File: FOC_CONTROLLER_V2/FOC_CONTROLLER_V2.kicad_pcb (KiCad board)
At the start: 4 copper layers, 80 x 60 mm, 124 parts, among them IC1 STSPIN32G4, J1 DC IN, J2 Conn_01x01, J3 Conn_01x01, J4 Conn_01x01, J5 ENCODER, J6 JTAG, Q1 CSD18502Q5B, Q2 CSD18502Q5B, Q3 CSD18502Q5B, Q4 CSD18502Q5B, Q5 CSD18502Q5B, Q6 CSD18502Q5B, SW3 SW_DIP_x02, U1 THVD1520

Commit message: Routage Phases PCB
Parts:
- removed C23: N.M., Capacitor_SMD:C_0603_1608Metric
- removed the R14 at (70.7, 79.0)
- removed the R15 at (70.7, 81.5)
- removed the R16 at (70.7, 84.0)
- removed the R17 at (70.7, 86.5)
- removed the R18 at (70.7, 89.0)
- removed Rshunt1, Rshunt2, Rshunt3: 7m, Resistor_SMD:R_2512_6332Metric_Pad1.40x3.35mm_HandSolder
- removed TP1, TP2, TP21, TP3, TP4: 3V3, TestPoint:TestPoint_Pad_D1.0mm
- removed TP10, TP11, TP12, TP13, TP14, TP15, TP16, TP17, TP18, TP20, TP5, TP6, TP7, TP8, TP9: 5V, TestPoint:TestPoint_Pad_D1.0mm
- removed TP19: 24V, TestPoint:TestPoint_Pad_D1.0mm
- added C25: N.M., Capacitor_SMD:C_1210_3225Metric_Pad1.33x2.70mm_HandSolder, B.Cu at (156.2, 85.1)
- added C26: N.M., Capacitor_SMD:C_1210_3225Metric_Pad1.33x2.70mm_HandSolder, B.Cu at (140.6, 85.1)
- added C27: N.M., Capacitor_SMD:C_1210_3225Metric_Pad1.33x2.70mm_HandSolder, B.Cu at (135.6, 88.3)
- added C28: 100n, Capacitor_SMD:C_0603_1608Metric, F.Cu at (141.8, 111.1)
- added C29: 100n, Capacitor_SMD:C_0603_1608Metric, F.Cu at (220.7, 71.0)
- added C30: 220n, Capacitor_SMD:C_0603_1608Metric, F.Cu at (220.7, 73.5)
- added C31: N.M., Capacitor_SMD:C_1210_3225Metric_Pad1.33x2.70mm_HandSolder, B.Cu at (146.2, 85.1)
- added C32: N.M., Capacitor_SMD:C_1210_3225Metric_Pad1.33x2.70mm_HandSolder, B.Cu at (130.5, 85.1)
- added C33: N.M., Capacitor_SMD:C_1210_3225Metric_Pad1.33x2.70mm_HandSolder, B.Cu at (151.2, 85.1)
- added C34: N.M., Capacitor_SMD:C_1210_3225Metric_Pad1.33x2.70mm_HandSolder, B.Cu at (146.2, 88.3)
- added D4: STPS0560Z, Diode_SMD:D_SOD-123, F.Cu at (158.3, 108.8)
- added J10: R-78B5.0-2.0, Package_TO_SOT_SMD:SOT-223, F.Cu at (130.1, 128.6)
- added J7: Conn_SW_2, Connector_JST:JST_GH_SM02B-GHS-TB_1x02-1MP_P1.25mm_Horizontal, F.Cu at (196.1, 94.5)
- added J8: Conn_SW_2, Connector_JST:JST_GH_SM02B-GHS-TB_1x02-1MP_P1.25mm_Horizontal, F.Cu at (188.3, 108.2)
- added J9: USB_C_Receptacle_USB2.0_14P, Connector_USB:USB_C_Receptacle_G-Switch_GT-USB-7010ASV, F.Cu at (103.6, 116.6)
- added JP1: SolderJumper_3_Open, Jumper:SolderJumper-3_P1.3mm_Open_RoundedPad1.0x1.5mm_NumberLabels, F.Cu at (126.3, 121.9)
- added L1: 15u, Footprint:L_Wurth_WE-MXGI-5030, F.Cu at (159.3, 113.1)
- added R14: 30K, Resistor_SMD:R_0603_1608Metric, F.Cu at (133.5, 84.6)
- added R14: 30K, Resistor_SMD:R_0603_1608Metric, F.Cu at (267.0, 84.4)
- added R15: 30K, Resistor_SMD:R_0603_1608Metric, F.Cu at (265.4, 87.4)
- added R15: 30K, Resistor_SMD:R_0603_1608Metric, F.Cu at (132.0, 87.6)
- added R16: 1.5k, Resistor_SMD:R_0603_1608Metric, F.Cu at (130.4, 84.6)
- added R16: 1.5k, Resistor_SMD:R_0603_1608Metric, F.Cu at (263.8, 84.4)
- added R17: 15k, Resistor_SMD:R_0603_1608Metric, F.Cu at (263.8, 87.4)
- added R17: 15k, Resistor_SMD:R_0603_1608Metric, F.Cu at (130.4, 87.6)
- added R18: 1.5k, Resistor_SMD:R_0603_1608Metric, F.Cu at (132.0, 84.6)
- added R18: 1.5k, Resistor_SMD:R_0603_1608Metric, F.Cu at (265.4, 84.4)
- added R49: 100k, Capacitor_SMD:C_0603_1608Metric, F.Cu at (145.0, 111.1)
- added R50: 200, Capacitor_SMD:C_0603_1608Metric, F.Cu at (145.0, 113.6)
- added R51: 100k, Capacitor_SMD:C_0603_1608Metric, F.Cu at (228.8, 73.5)
- added R52: 200, Capacitor_SMD:C_0603_1608Metric, F.Cu at (228.8, 76.0)
- added R53: 10, Resistor_SMD:R_0603_1608Metric, F.Cu at (115.5, 116.6)
- C1, C3, C5: footprint Capacitor_SMD:C_0603_1608Metric -> Capacitor_SMD:C_0805_2012Metric
- C13: value N.M. -> 10u
- C17: footprint Capacitor_SMD:C_0201_0603Metric -> Capacitor_SMD:C_0603_1608Metric
- C19: value 4u7 -> 10u; footprint Capacitor_SMD:C_1210_3225Metric -> Capacitor_SMD:C_0805_2012Metric_Pad1.18x1.45mm_HandSolder
- C20: value 4u7 -> 22u; footprint Capacitor_SMD:C_1210_3225Metric -> Capacitor_SMD:C_0805_2012Metric_Pad1.18x1.45mm_HandSolder
- C21: value 1u -> N.M.; footprint Capacitor_SMD:C_0603_1608Metric -> Capacitor_SMD:C_1210_3225Metric_Pad1.33x2.70mm_HandSolder; moved to B.Cu
- C22: value 47u -> N.M.; footprint Capacitor_SMD:C_0603_1608Metric -> Capacitor_SMD:C_1210_3225Metric_Pad1.33x2.70mm_HandSolder; moved to B.Cu
- C4, C6, C7: value 220n 100V -> 220n; footprint Capacitor_SMD:C_0805_2012Metric -> Capacitor_SMD:C_1210_3225Metric_Pad1.33x2.70mm_HandSolder; moved to B.Cu
- J2, J3, J4: footprint Footprint:REDCUBE SMT -> Footprint:REDCUBETHT_74651173R
- J5: footprint Connector_JST:JST_SH_SM04B-SRSS-TB_1x04-1MP_P1.00mm_Horizontal -> Connector_JST:JST_GH_SM04B-GHS-TB_1x04-1MP_P1.25mm_Horizontal
- Q1, Q4, Q6: value CSD18502Q5B -> CSD18543Q3A; moved to B.Cu
- Q2, Q3, Q5: value CSD18502Q5B -> CSD19534Q5A; moved to B.Cu
- R31: value 5k6 -> R_Shunt; footprint Resistor_SMD:R_0402_1005Metric -> shunt:R_2512_6332Metric_Pad1.40x3.35mm_HandSolder
- R32: value 402k -> R_Shunt; footprint Resistor_SMD:R_0402_1005Metric -> shunt:R_2512_6332Metric_Pad1.40x3.35mm_HandSolder
- R33: value 80k6 -> R_Shunt; footprint Resistor_SMD:R_0402_1005Metric -> shunt:R_2512_6332Metric_Pad1.40x3.35mm_HandSolder
- U1: value THVD1520 -> THVD1400
- moved R38 205.3 mm to (236.3, 84.0)
- moved R39 205.3 mm to (236.3, 86.0)
- moved R40 203.1 mm to (236.3, 88.0)
- moved C18 202.7 mm to (216.7, 83.6)
- moved NTC1 202.7 mm to (220.7, 76.0)
- moved R2 202.7 mm to (220.7, 78.6)
- moved R8 202.7 mm to (220.7, 81.1)
- moved R9 202.7 mm to (220.7, 83.6)
- moved C10 202.7 mm to (216.7, 68.5)
- moved C11 202.7 mm to (216.7, 71.0)
- moved C12 202.7 mm to (216.7, 73.5)
- moved C14 202.7 mm to (216.7, 76.0)
- moved C15 202.7 mm to (216.7, 78.6)
- moved C9 202.7 mm to (216.7, 66.0)
- moved R10 202.7 mm to (224.8, 66.0)
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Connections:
- net A renamed /A
- net B renamed /B
- C13 pad 1: /OPN2 -> Net-(IC1-REGIN)
- C13 pad 2: /OPO2 -> GND
- C16 pad 1: /OPN3 -> Net-(IC1-REGIN)
- C16 pad 2: /OPO3 -> GND
- C19 pad 1: +24V -> +5V
- C2 pad 1: +24V -> +48V
- C20 pad 1: +24V -> +3,3V_EXT
- C21 pad 1: Net-(PS1-VCC) -> GND
- C21 pad 2: Net-(PS1-AGND) -> +48V
- C22 pad 1: +5V -> GND
- C22 pad 2: Net-(PS1-AGND) -> +48V
- C4 pad 2: +24V -> +48V
- C6 pad 2: +24V -> +48V
- C7 pad 2: +24V -> +48V
- C8 pad 1: +24V -> +48V
- IC1 pad 14: /OPP1 -> /OPP3
- IC1 pad 15: /OPO1 -> /OPO3
- IC1 pad 16: /OPN1 -> /OPN3
- IC1 pad 23: /OPP3 -> /OPP1
- IC1 pad 24: /OPO3 -> /OPO1
- IC1 pad 25: /OPN3 -> /OPN1
- IC1 pad 59: unconnected-(IC1-PB8-Pad59) -> /L_SW_2
- IC1 pad 60: unconnected-(IC1-PB9-Pad60) -> /L_SW_1
- IC1 pad 61: +24V -> +48V
- IC1 pad 62: +24V -> /SW
- IC1 pad 63: +5V -> Net-(IC1-REGIN)
- IC1 pad 64: +5V -> Net-(IC1-REGIN)
- J1 pad 1: +24V -> +48V
- Q1 pad 1: /Ampli_1/VSHUNTXP -> Net-(Q1-S-Pad1)
- Q1 pad 2: /Ampli_1/VSHUNTXP -> Net-(Q1-S-Pad1)
- Q1 pad 3: /Ampli_1/VSHUNTXP -> Net-(Q1-S-Pad1)
- Q2 pad 5: +24V -> +48V
- Q3 pad 5: +24V -> +48V
- Q4 pad 1: /Ampli_2/VSHUNTXP -> Net-(Q4-S-Pad1)
- Q4 pad 2: /Ampli_2/VSHUNTXP -> Net-(Q4-S-Pad1)
- Q4 pad 3: /Ampli_2/VSHUNTXP -> Net-(Q4-S-Pad1)
- Q5 pad 5: +24V -> +48V
- Q6 pad 1: /Ampli_3/VSHUNTXP -> Net-(Q6-S-Pad1)
- Q6 pad 2: /Ampli_3/VSHUNTXP -> Net-(Q6-S-Pad1)
- Q6 pad 3: /Ampli_3/VSHUNTXP -> Net-(Q6-S-Pad1)
- R13 pad 1: GND -> /Ampli_2/VSHUNTXN
- R23 pad 1: GND -> /Ampli_3/VSHUNTXN
- R28 pad 1: +24V -> +48V
- R31 pad 1: Net-(PS1-FSW) -> GND
- R31 pad 2: Net-(PS1-AGND) -> /Ampli_1/VSHUNTXN
- R32 pad 1: +5V -> GND
- R32 pad 2: Net-(PS1-FB) -> /Ampli_2/VSHUNTXN
- R33 pad 1: Net-(PS1-FB) -> GND
- R33 pad 2: Net-(PS1-AGND) -> /Ampli_3/VSHUNTXN
- U1 pad 8: +5V -> Net-(JP1-C)
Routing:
- net /OUT3: track 0.00 -> 39.3 mm, vias 0 -> 1
- net GND: track 0.00 -> 36.4 mm, vias 0 -> 30
- net /OUT2: track 0.00 -> 29.2 mm, vias 0 -> 1
- net /OUT1: track 0.00 -> 20.1 mm, vias 0 -> 1
- net /A: track 0.00 -> 16.1 mm
- net /B: track 0.00 -> 15.6 mm, vias 0 -> 2
- net /GHS2: track 0.00 -> 14.5 mm, vias 0 -> 1
- net /Ampli_3/VSHUNTXP: track 0.00 -> 14.3 mm
- net /Ampli_3/VSHUNTXN: track 0.00 -> 11.9 mm
- net /Ampli_2/VSHUNTXP: track 0.00 -> 7.91 mm
- net /Ampli_2/VSHUNTXN: track 0.00 -> 7.71 mm
- net /Ampli_1/VSHUNTXP: track 0.00 -> 6.86 mm
- net Net-(JP1-C): track 0.00 -> 6.44 mm
- net +3,3V_EXT: track 0.00 -> 6.37 mm
- net /Ampli_1/VSHUNTXN: track 0.00 -> 4.52 mm
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- added copper zone on B.Cu, net +48V
- added copper zone on B.Cu, net /OUT1
- added copper zone on B.Cu, net /OUT2
- added copper zone on B.Cu, net /OUT3
- added copper zone on F.Cu, net GND
- added copper zone on In1.Cu, net GND
- added copper zone on In2.Cu, net GND
- added copper zone on B.Cu, net Net-(Q1-S-Pad1)
- added copper zone on F.Cu, net Net-(Q1-S-Pad1)
- added copper zone on B.Cu, net Net-(Q4-S-Pad1)
- added copper zone on F.Cu, net Net-(Q4-S-Pad1)
- added copper zone on B.Cu, net Net-(Q6-S-Pad1)
- added copper zone on F.Cu, net Net-(Q6-S-Pad1)
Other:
- board size 80 x 60 mm -> 80 x 80 mm

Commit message: Routage PCB 99%
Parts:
- removed C25, C34: N.M., Capacitor_SMD:C_1210_3225Metric_Pad1.33x2.70mm_HandSolder
- removed C7: 220n, Capacitor_SMD:C_1210_3225Metric_Pad1.33x2.70mm_HandSolder
- removed the R14 at (267.0, 84.4)
- removed the R15 at (265.4, 87.4)
- removed the R16 at (263.8, 84.4)
- removed the R17 at (263.8, 87.4)
- removed the R18 at (265.4, 84.4)
- C2: footprint Capacitor_SMD:CP_Elec_10x10.5 -> Capacitor_SMD:CP_Elec_18x22
- C21, C22, C26, C27, C31, C32, C33, C4, C6: moved to F.Cu
- J10: value R-78B5.0-2.0 -> AZ1117
- moved R48 136.1 mm to (108.8, 130.4), turned to 180 degrees
- moved D3 134.4 mm to (105.6, 130.4)
- moved D1 133.9 mm to (105.6, 126.2)
- moved R11 129.5 mm to (108.8, 126.2), turned to 180 degrees
- moved D5 128.0 mm to (107.8, 62.1), turned to 180 degrees
- moved R40 127.6 mm to (111.3, 62.1)
- moved R38 105.0 mm to (143.6, 133.5)
- moved C30 104.8 mm to (128.6, 123.5)
- moved C8 101.6 mm to (142.7, 114.0), turned to -90 degrees
- moved D8 101.5 mm to (140.1, 133.5), turned to 180 degrees
- moved R35 99.7 mm to (130.5, 116.0)
- moved R10 99.2 mm to (138.3, 114.6), turned to 90 degrees
- moved R39 98.9 mm to (149.5, 133.5), turned to 180 degrees
- moved R34 98.4 mm to (133.3, 117.5)
- moved D9 88.8 mm to (153.0, 133.5)
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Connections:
- D5 pad 2: +24V -> +48V
- IC1 pad 47: /DRIVE_EN -> /RECIEVE_EN
- IC1 pad 48: /RECIEVE_EN -> /DRIVE_EN
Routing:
- net /VCP_RX: track 0.00 -> 82.2 mm, vias 0 -> 2
- net /VCP_TX: track 0.00 -> 76.6 mm, vias 0 -> 2
- net Net-(IC1-PB3): track 0.00 -> 65.7 mm, vias 0 -> 2
- net Net-(IC1-PB5): track 0.00 -> 64.5 mm, vias 0 -> 2
- net Net-(IC1-PD2): track 0.00 -> 64.3 mm, vias 0 -> 2
- net /NTC: track 0.00 -> 63.7 mm, vias 0 -> 2
- net Net-(Q2-G): track 1.09 -> 64.5 mm, vias 0 -> 2
- net Net-(IC1-PB4): track 0.00 -> 59.9 mm, vias 0 -> 2
- net Net-(IC1-PC15): track 0.00 -> 55.5 mm, vias 0 -> 2
- net /NRST: track 0.00 -> 52.2 mm, vias 0 -> 2
- net Net-(Q5-G): track 0.00 -> 50.8 mm, vias 0 -> 2
- net Net-(Q3-G): track 0.00 -> 49.7 mm, vias 0 -> 2
- net Net-(IC1-PC14): track 0.00 -> 48.0 mm, vias 0 -> 2
- net /L_SW_1: track 0.00 -> 46.1 mm, vias 0 -> 2
- net /OUT2: track 29.2 -> 73.8 mm
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- added copper zone on B.Cu, net +3.3V
- added copper zone on F.Cu, net +3.3V
- added copper zone on F.Cu, net +48V
- added copper zone on B.Cu, net +5V
- added copper zone on F.Cu, net +5V
- added copper zone on F.Cu, net /SW
- added copper zone on F.Cu, net Net-(IC1-REGIN)
- added copper zone on F.Cu, net Net-(IC1-SCREF)

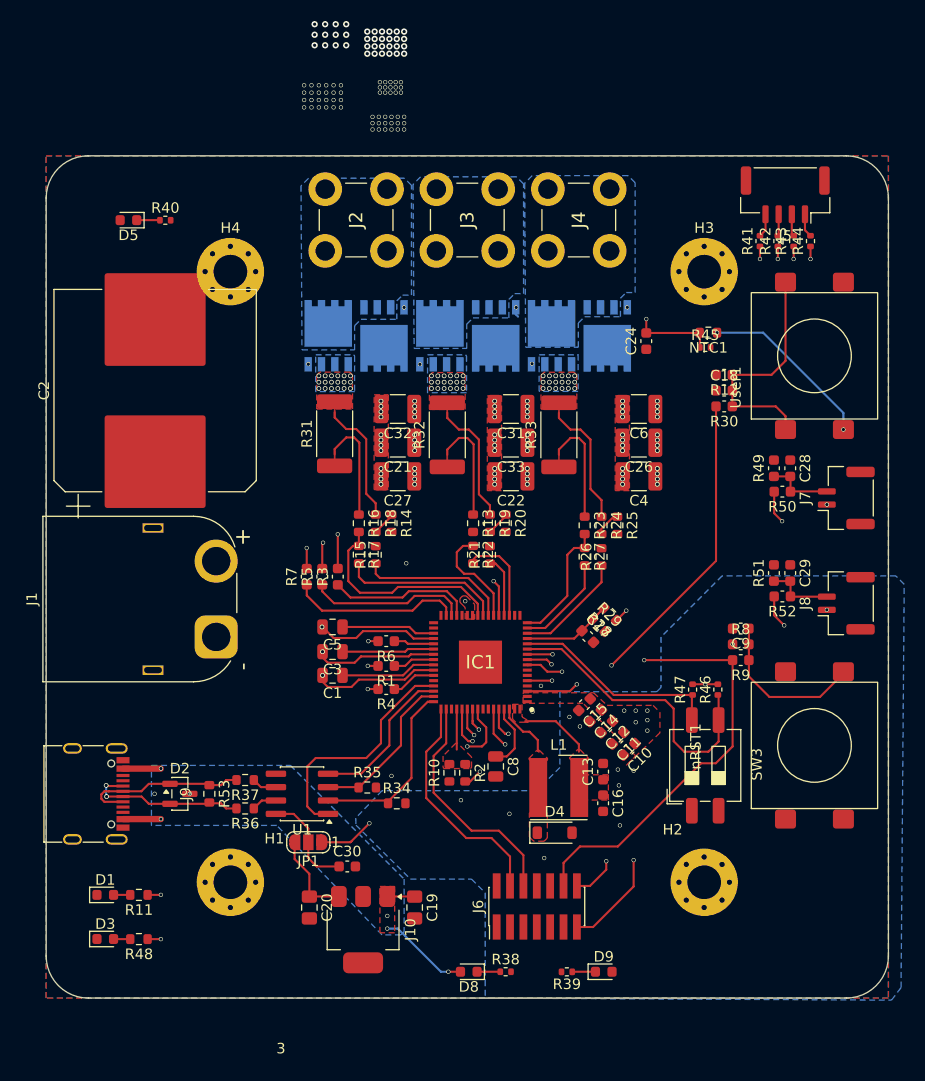
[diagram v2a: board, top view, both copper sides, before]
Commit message: PCB driver
Routage terminé
Verifier si l'USB C permet d'avoir un bus et non pas une topologie en étoile
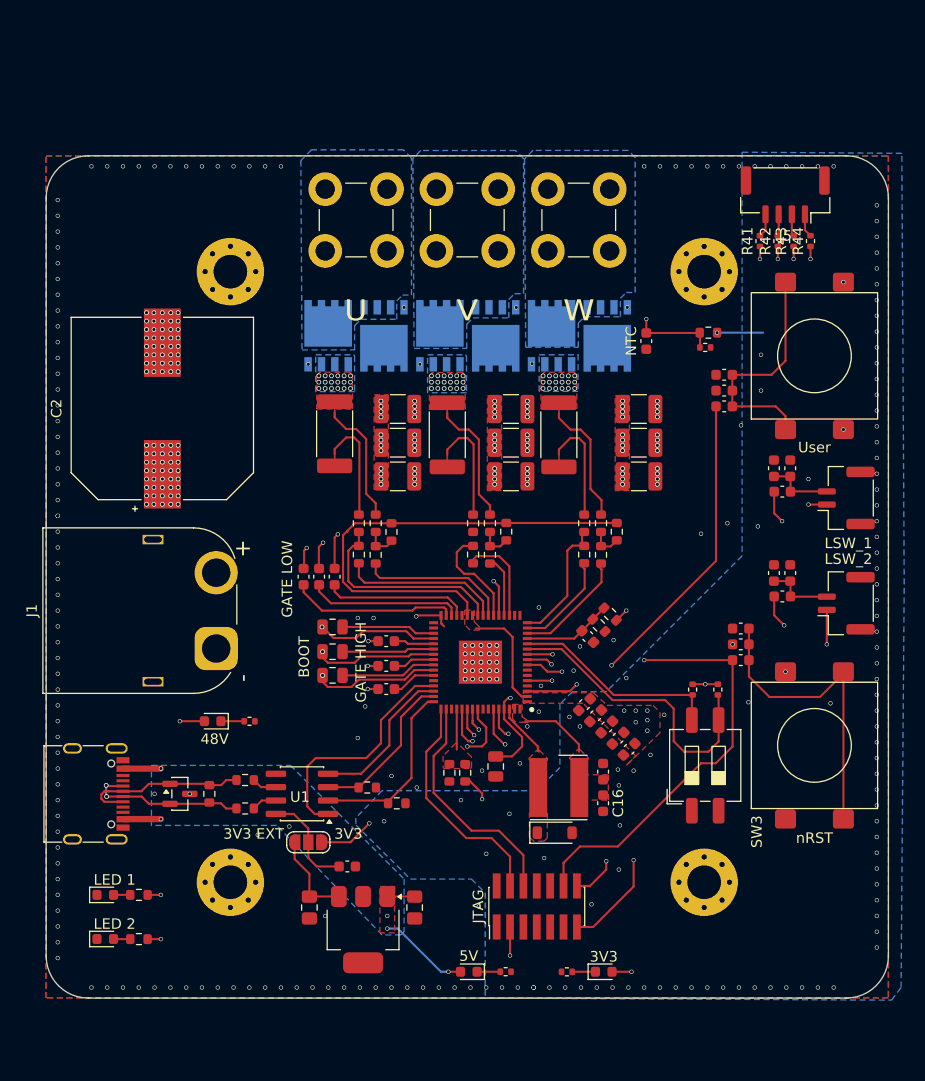
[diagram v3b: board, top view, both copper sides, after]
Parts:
- 3V3 EXT: renamed from H1
- C2: footprint Capacitor_SMD:CP_Elec_18x22 -> Footprint:CP_Wurth_WCAP-ASLL-D16L17
- GATE HIGH: renamed from R4
- LED 1: renamed from D1
- LED 2: renamed from D3
- moved D5 48.3 mm to (115.8, 109.7)
- moved R40 48.3 mm to (119.3, 109.7)
- moved C2 1.83 mm to (111.0, 80.0)
- moved J1 1.10 mm to (116.2, 102.8)
- moved R14 0.82 mm to (132.8, 91.7), turned to 90 degrees
- moved R20 0.80 mm to (143.7, 91.7), turned to 90 degrees
- moved R25 0.60 mm to (154.2, 91.7), turned to 90 degrees
- moved R7 0.30 mm to (124.4, 96.0)
- moved R3 0.30 mm to (127.4, 96.0)
- moved R5 0.30 mm to (125.9, 96.0)
- moved R27 0.21 mm to (151.1, 93.9)
- moved R23 0.21 mm to (151.1, 90.9)
- moved R24 0.21 mm to (152.7, 90.9)
- moved R26 0.21 mm to (152.7, 93.9)
- renumbered D9 to 3V3, D8 to 5V, C1 to BOOT, J6 to JTAG, J7 to LSW_1, J8 to LSW_2, C24 to NTC, J2 to U, User1 to User, J3 to V, nRST1 to nRST
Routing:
- net +3.3V: track 26.2 -> 79.5 mm, vias 15 -> 17
- net Net-(C9-Pad1): track 15.4 -> 29.4 mm
- net Net-(IC1-PB5): track 64.5 -> 72.6 mm
- net Net-(IC1-PB3): track 65.7 -> 73.4 mm
- net +48V: track 7.60 -> 12.2 mm, vias 37 -> 79
- net GND: track 0.00 -> 3.57 mm, vias 50 -> 321
- net Net-(Q6-G): track 37.0 -> 38.6 mm
- net Net-(Q2-G): track 64.5 -> 63.4 mm
- net Net-(R19-Pad2): track 2.27 -> 3.15 mm
- net Net-(R14-Pad1): track 2.27 -> 3.13 mm
- net Net-(R24-Pad2): track 2.27 -> 3.10 mm
- net Net-(IC1-PC14): track 48.0 -> 47.4 mm
- net /GLS3: track 16.3 -> 15.7 mm
- net Net-(IC1-PC15): track 55.5 -> 55.0 mm
- net /GLS2: track 15.1 -> 14.6 mm
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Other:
- board text added: "48V"
- board text added: "GATE LOW"
- board text added: "U"
- board text added: "W"

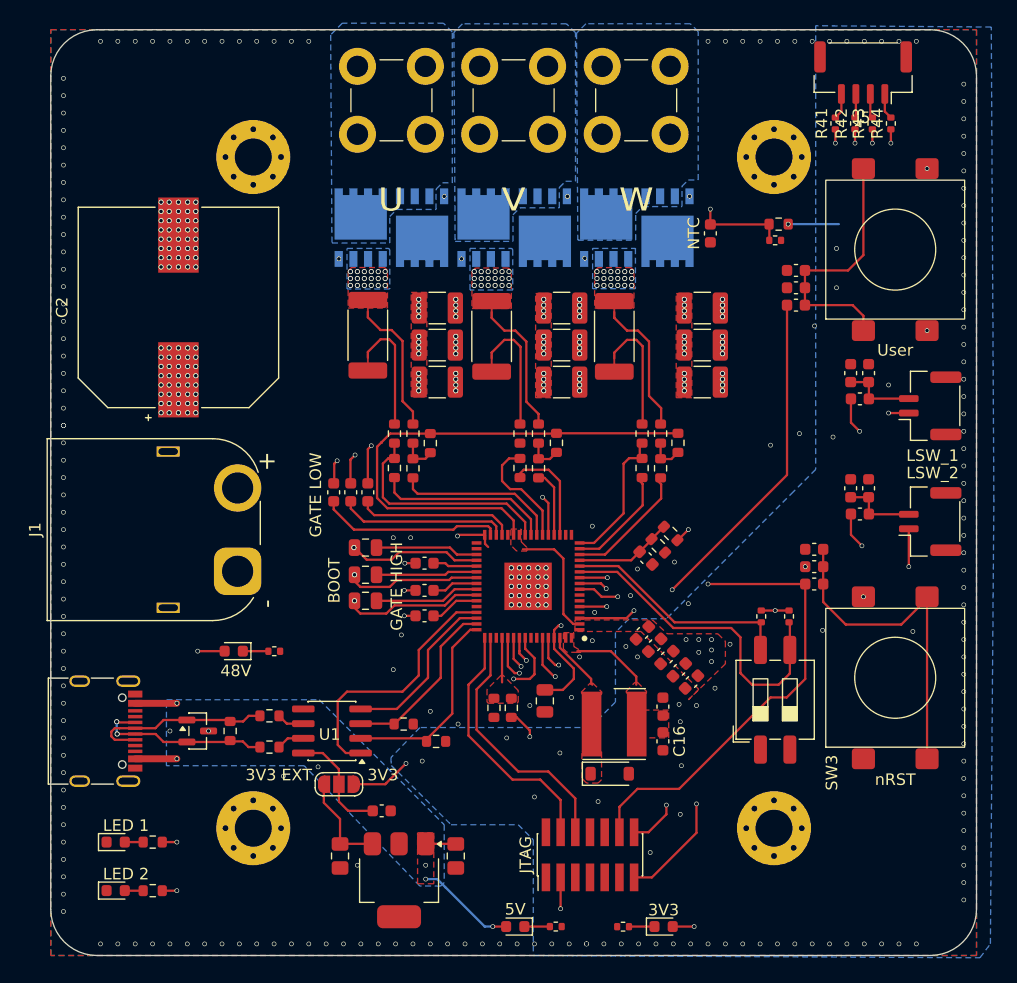
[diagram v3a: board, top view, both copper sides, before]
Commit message: PCB driver : DONE
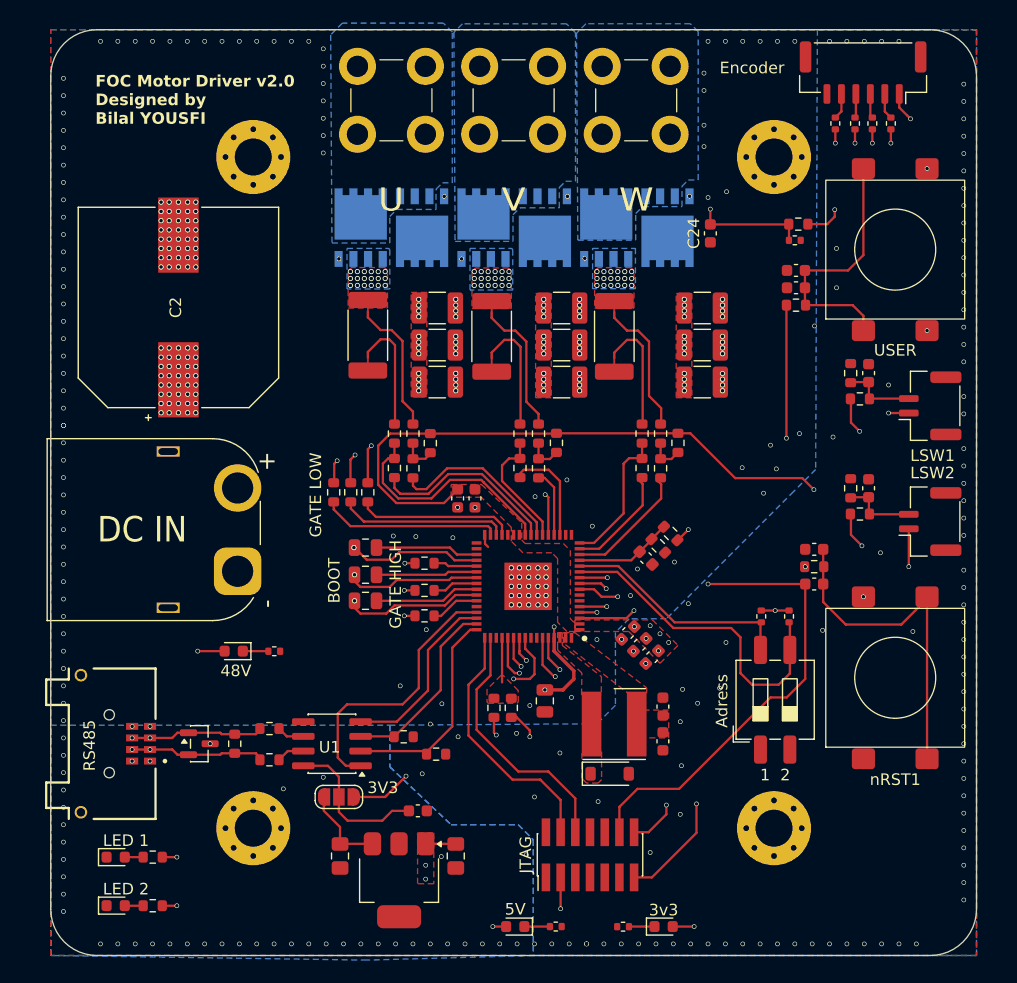
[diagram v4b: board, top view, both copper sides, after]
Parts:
- removed J5: ENCODER, Connector_JST:JST_GH_SM04B-GHS-TB_1x04-1MP_P1.25mm_Horizontal
- removed J9: USB_C_Receptacle_USB2.0_14P, Connector_USB:USB_C_Receptacle_G-Switch_GT-USB-7010ASV
- added G***: LOGO, LOGO, B.Cu at (229.5, 104.9)
- added G***: LOGO, LOGO, B.Cu at (146.4, 109.5)
- added J11: T1M-04-GF-DH, Footprint:SAMTEC_T1M-04-GF-DH, F.Cu at (107.8, 117.7)
- added J12: Conn_01x06, Connector_JST:JST_GH_SM06B-GHS-TB_1x06-1MP_P1.25mm_Horizontal, F.Cu at (170.2, 59.7)
- 1  2: renamed from C16
- DC IN: renamed from J1
- GATE HIGH: renamed from R6; footprint Capacitor_SMD:C_0603_1608Metric -> Resistor_SMD:R_0603_1608Metric
- R1, R3, R30, R49, R5, R50, R51, R52, R7, R8: footprint Capacitor_SMD:C_0603_1608Metric -> Resistor_SMD:R_0603_1608Metric
- R4: renamed from GATE HIGH; footprint Capacitor_SMD:C_0603_1608Metric -> Resistor_SMD:R_0603_1608Metric
- RS485: renamed from 3V3 EXT
- moved C10 25.7 mm to (135.2, 96.5), turned to -90 degrees
- moved C14 20.1 mm to (136.7, 96.5), turned to -90 degrees
- moved C30 3.12 mm to (131.7, 123.5)
- moved C11 2.60 mm to (152.0, 110.2)
- moved C12 2.60 mm to (150.9, 109.2)
- moved R45 1.70 mm to (164.3, 74.2)
- moved NTC1 1.70 mm to (164.6, 72.8)
- moved LED 2 1.30 mm to (105.6, 131.7)
- moved LED 1 1.30 mm to (105.6, 127.5)
- moved R11 1.30 mm to (108.8, 127.5)
- moved R48 1.30 mm to (108.8, 131.7)
- moved C15 1.25 mm to (149.9, 108.1)
- moved R53 1.17 mm to (115.9, 117.7)
- moved D2 1.11 mm to (112.8, 117.7)
- moved R36 1.10 mm to (118.9, 119.1)
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- renumbered 3V3 to 3v3, SW3 to Adress, NTC to C24, R44 to Encoder, U to J2, LSW_1 to LSW1, LSW_2 to LSW2, JP1 to PwrJumper1, User to USER, nRST to nRST1
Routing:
- net GND: track 3.57 -> 121.9 mm, vias 321 -> 340
- net +5V: track 18.5 -> 3.76 mm
- net Net-(IC1-REGIN): track 6.71 -> 0.00 mm
- net /SW: track 5.21 -> 0.00 mm
- net /A: track 16.1 -> 11.6 mm, vias 0 -> 2
- net Net-(Q2-G): track 63.4 -> 59.0 mm
- net /B: track 15.6 -> 11.6 mm
- net Net-(PwrJumper1-C): track 9.71 -> 13.2 mm
- net Net-(IC1-PC14): track 47.4 -> 50.4 mm
- net /NTC: track 63.7 -> 66.6 mm
- net /User: track 38.0 -> 40.2 mm
- net +3.3V: track 79.5 -> 77.5 mm, vias 17 -> 19
- net /OUT2: track 73.8 -> 72.0 mm
- net Net-(Q4-G): track 24.8 -> 26.4 mm
- net Net-(Q6-G): track 38.6 -> 37.2 mm
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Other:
- board text added: "FOC Motor Driver v2.0 Designed by Bilal YOUSFI"

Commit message: PCB driver : Graphics
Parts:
- removed the G*** at (229.5, 104.9)
- removed the G*** at (146.4, 109.5)
- added G***: LOGO, LOGO, F.Cu at (169.1, 130.3)
- added G***: LOGO, LOGO, B.Cu at (148.4, 107.3)
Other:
- board text added: "Motion System"
- board text added: "TDI"
